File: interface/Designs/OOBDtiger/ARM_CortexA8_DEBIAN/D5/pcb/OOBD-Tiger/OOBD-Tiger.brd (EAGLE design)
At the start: 63.4 x 38.2 mm, 123 parts, among them IC1 ADM3053M, IC2 ADM3053M, IC4 DS3231, U1 SY6280, U10 MP1482DS, U2 SN65HVD230(SO8), U3 SY6280, U6 SN65HVD230(SO8)

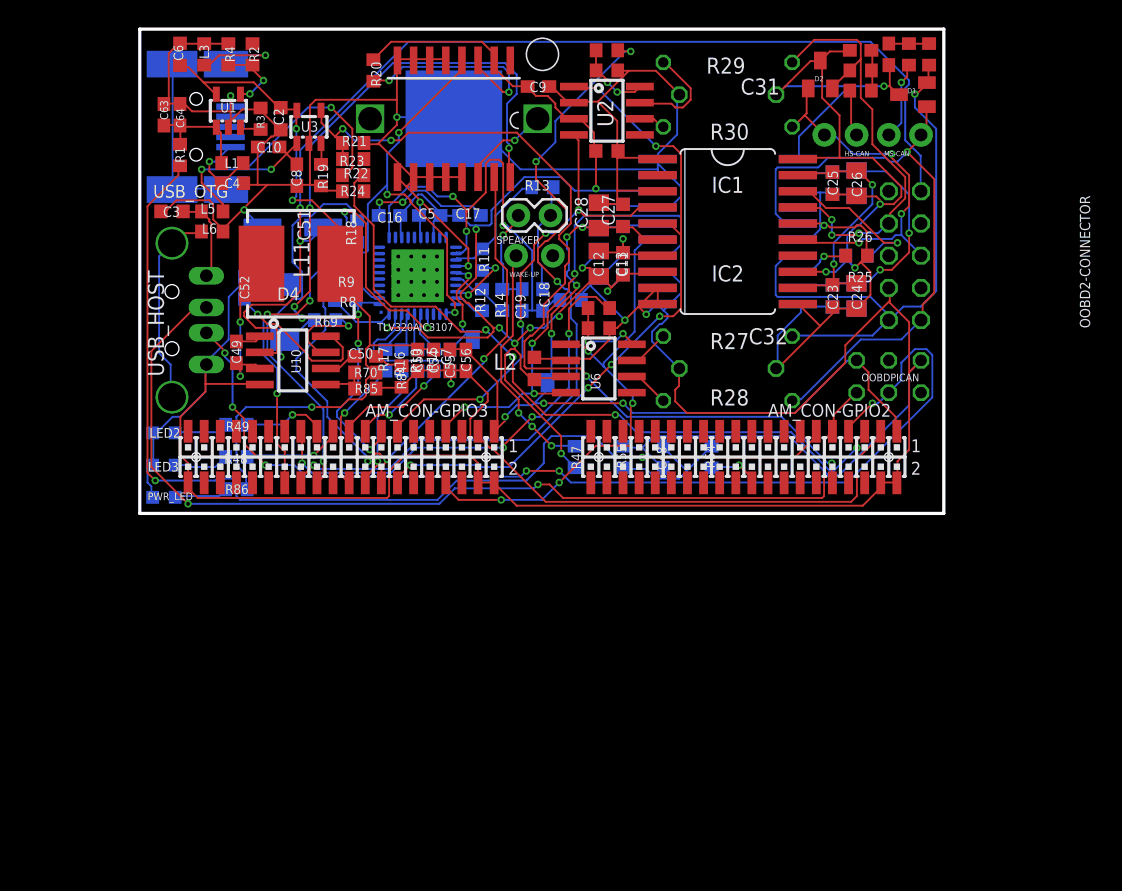
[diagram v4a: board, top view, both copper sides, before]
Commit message: add missing 1V8 LDO (97,1% autorouting now)
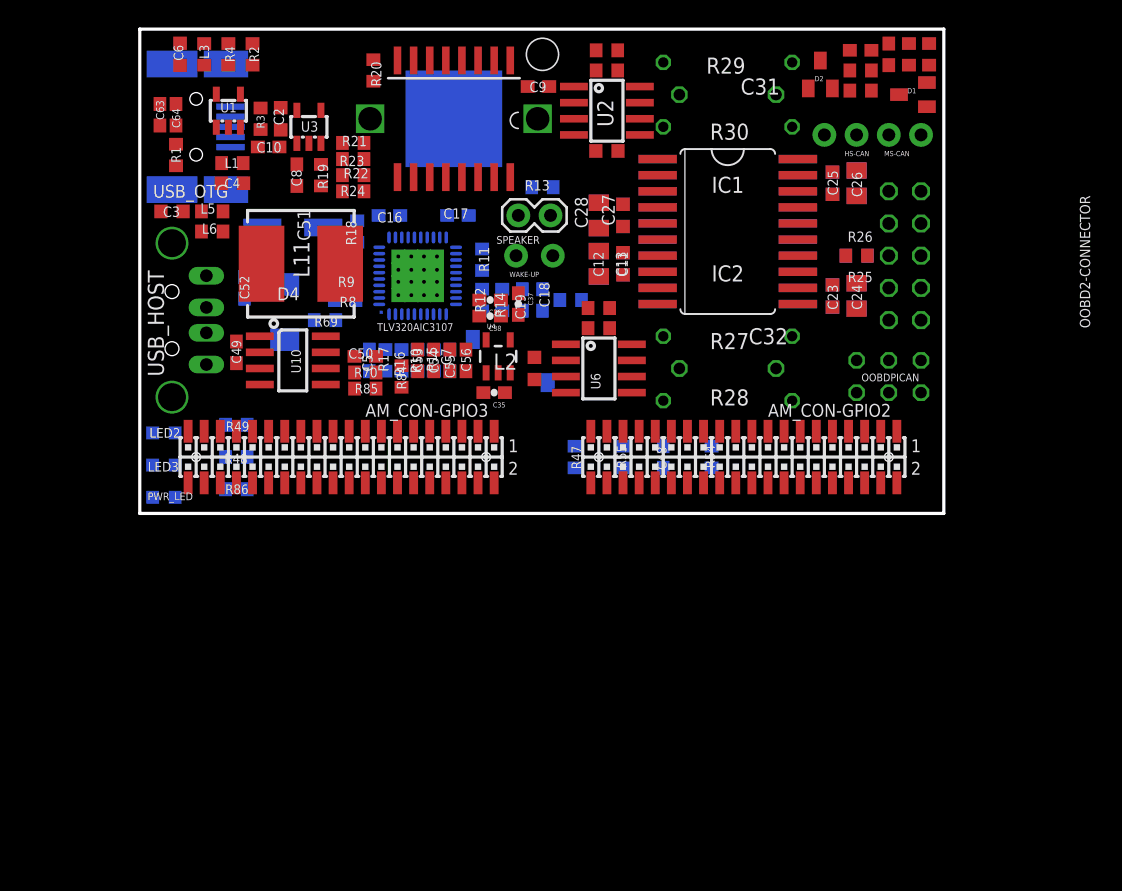
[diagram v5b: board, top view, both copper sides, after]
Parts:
- added C35: 1µf, SparkFun-Passives:0603-CAP
- added C36: 2.2µf, SparkFun-Passives:0603-CAP
- added C37: NA (47pF), SparkFun-Passives:0603-CAP
- added C38: 47pF, SparkFun-Passives:0603-CAP
- added U4: TLV70215, SparkFun-PowerIC:SOT23-5
- C16: value 22µf -> 47pF
- C17: value 0.1µf -> 47pF
- moved C5 12.4 mm to (18.1, 12.1), turned to 90 degrees
- moved C17 0.95 mm to (25.1, 23.5)
- moved C63 0.32 mm to (1.59, 31.4)
- moved C64 0.32 mm to (2.86, 31.4)
- moved R1 0.32 mm to (2.86, 28.3)
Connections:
- removed net N$16: C16.2, C17.2
- new net DVDD: C36.2, C38.2, TLV320AIC3107.33, U4.5
- new net N$12: C37.2, U4.4
- net +3V3: now also C35.2, TLV320AIC3107.12, TLV320AIC3107.21, U4.1, U4.3
- net GND: now also C16.2, C17.2, C35.1, C36.1, C37.1, C38.1, U4.2
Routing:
- net GND: track 427.8 -> 0.00 mm, vias 9 -> 0
- net +5V: track 139.7 -> 0.00 mm, vias 10 -> 0
- net +3V3: track 122.5 -> 0.00 mm, vias 10 -> 0
- net GNDA: track 108.6 -> 0.00 mm, vias 5 -> 0
- net +12V: track 92.1 -> 0.00 mm, vias 3 -> 0
- net USB0_VBUS: track 84.4 -> 0.00 mm, vias 2 -> 0
- net USB1_DP: track 82.5 -> 0.00 mm, vias 6 -> 0
- net USB1_DM: track 79.5 -> 0.00 mm, vias 2 -> 0
- net USB1_DRV: track 71.3 -> 0.00 mm, vias 4 -> 0
- net I2C0-SCL: track 64.2 -> 0.00 mm, vias 7 -> 0
- net HS-CAN_RS: track 59.9 -> 0.00 mm, vias 4 -> 0
- net USB1_VBUS: track 57.7 -> 0.00 mm, vias 4 -> 0
- net SYS_RESETN: track 57.0 -> 0.00 mm, vias 6 -> 0
- net I2C0-SDA: track 54.2 -> 0.00 mm, vias 3 -> 0
- net DCAN1_TX: track 53.5 -> 0.00 mm, vias 6 -> 0
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
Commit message: Modification according 107EVM
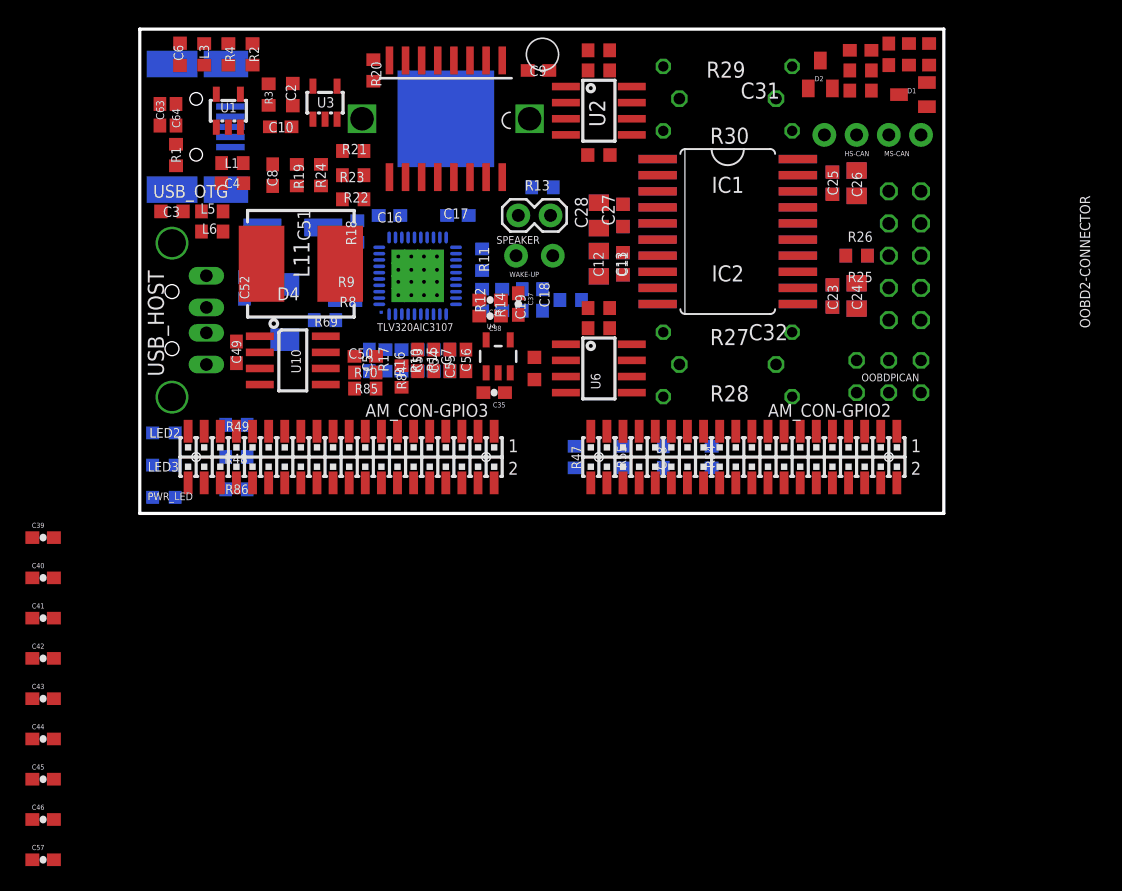
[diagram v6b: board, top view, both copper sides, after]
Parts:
- removed L2: (no value), inductor-neosid:SM-L15B
- added C39, C41, C45, C57: 0.1µF, SparkFun-Passives:0603-CAP
- added C40, C42, C43, C46: 10µF, SparkFun-Passives:0603-CAP
- added C44: 1.0µF, SparkFun-Passives:0603-CAP
- C16, C5: value 47pF -> 0.1µF
- C17: value 47pF -> 10µF
- C38: value 47pF -> 1.0µF
- C7: value 47pF -> 22µF
- moved R24 2.84 mm to (14.3, 26.7), turned to 90 degrees
- moved U3 2.29 mm to (14.6, 32.4)
- moved C2 2.13 mm to (12.1, 33.0)
- moved R3 2.01 mm to (10.2, 33.0)
- moved C8 1.91 mm to (10.5, 26.7)
- moved R22 1.91 mm to (16.8, 24.8)
- moved R19 1.90 mm to (12.4, 26.7)
- moved C10 1.85 mm to (11.1, 30.5)
- moved R23 1.27 mm to (16.8, 26.7)
- moved C9 1.27 mm to (31.4, 34.9)
- moved C1 0.71 mm to (36.2, 28.3)
- moved BAT2 0.64 mm to (24.1, 31.1)
- moved IC4 0.64 mm to (24.1, 31.1)
- moved R21 0.64 mm to (16.8, 28.6)
- moved R5 0.63 mm to (36.2, 34.9)
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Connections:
- removed net N$17: C7.2, L2.1, TLV320AIC3107.25
- new net GND1: C45.1, C46.1
- new net N$16: L4.1, SPEAKER.1
- net +3V3: now also C39.1, C40.1, C41.1, C42.1, C43.2; no longer TLV320AIC3107.40
- net +5V: now also C57.2, C7.2, TLV320AIC3107.25; no longer L2.2
- net AGND: no longer L4.2
- net DVDD: now also C44.2
- net GND: now also C39.2, C40.2, C41.2, C42.2, C43.1, C44.1, C57.1, R12.2, R14.1, TLV320AIC3107.26; no longer L4.1
- net N$14: now also L4.2; no longer SPEAKER.1
- net N$21: now also C45.2, C46.2, TLV320AIC3107.40; no longer R12.2, R14.1, TLV320AIC3107.26
